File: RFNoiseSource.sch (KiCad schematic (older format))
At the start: 46 parts, among them J1 Barrel_Jack, J2 Conn_Coaxial, J3 Conn_Coaxial, Q1 2SC3356, Q2 2SC3356, Q3 2SC3356, Q4 2SC3356, Q5 2SC3356, Q6 2SC3356, U1 AMS1117-3V3

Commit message: Added LCSC part numbers, added cutout notched, added series base resistors to emitter followers
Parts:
- added C14, C15, C16: 10 nF, Capacitors_SMD:C_0805_HandSoldering, symbol C_Small
- added R19, R21, R22, R24: NC, Resistors_SMD:R_0805_HandSoldering, symbol R
- added R20, R23: 0R, Resistors_SMD:R_0805_HandSoldering, symbol R
- added R25, R26, R27: 220R, Resistors_SMD:R_0805_HandSoldering, symbol R
- R1: value 1k -> 2k2; LCSC C17513 -> C17520
- R12, R4: value 10k -> 1k; LCSC C17414 -> C17513
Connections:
- net GND: now also C14.2, C15.2, C16.1, R19.2, R21.2, R22.2, R24.2
- net at Q3.1 (B), R9.1: now also R26.1; no longer C6.1
- net at C3.2, D1.2 (A), D2.2 (A)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: now also C16.2
- net at L2.2, Q4.2 (E): now also C15.1
- net at Q5.1 (B), R13.1: now also R27.1; no longer C9.1
- net at C11.1: now also R22.1, R23.1; no longer J3.1 (In)
- net at L1.2, Q1.2 (E): now also C14.1
- net at C8.1: now also R19.1, R20.1; no longer J2.1 (In)
- net at Q6.1 (B), R16.1: now also R25.1; no longer C12.1
- new net: C6.1, R26.2
- new net: C9.1, R27.2
- new net: J3.1 (In), R23.2, R24.1
- new net: J2.1 (In), R20.2, R21.1
- new net: C12.1, R25.2
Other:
- moved on the sheet: C10, C11, C6, C9, J2, J3, Q5, R11, R12, R13, R14, R15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

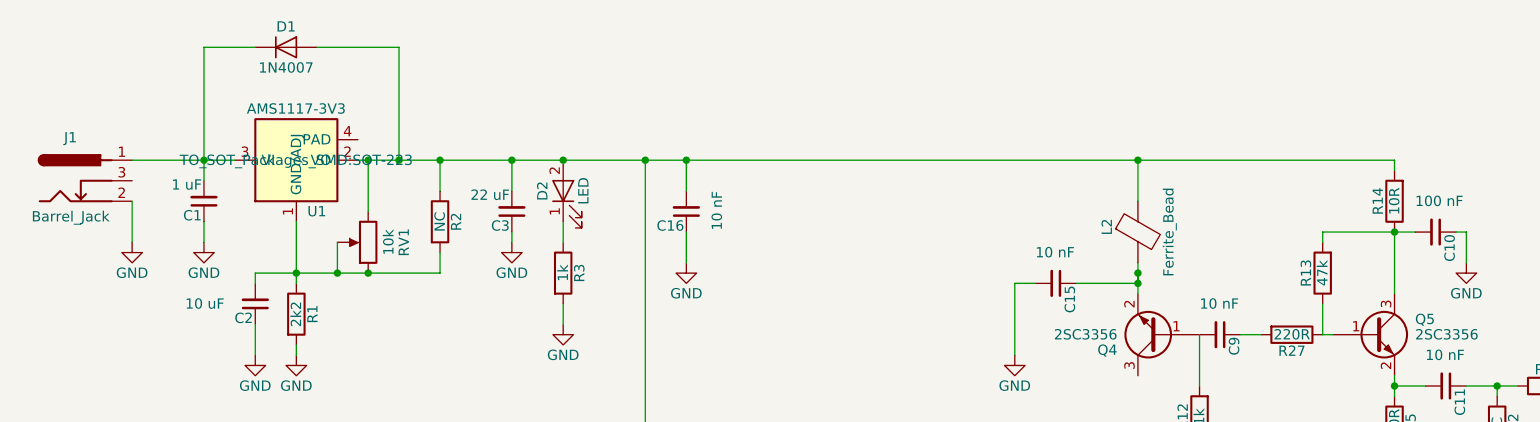
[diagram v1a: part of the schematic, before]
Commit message: Changed regulator
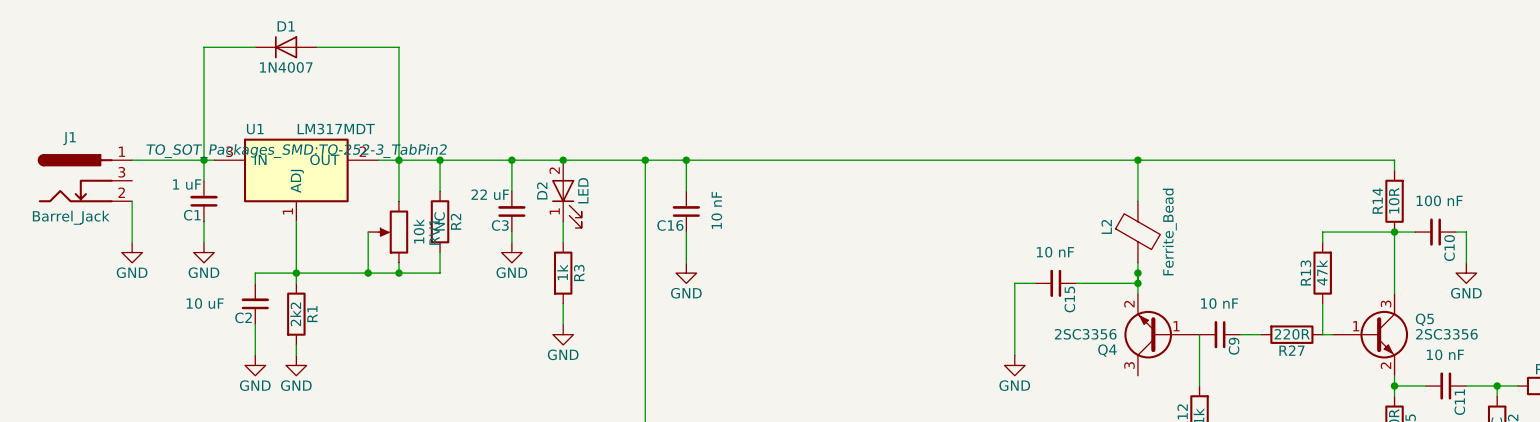
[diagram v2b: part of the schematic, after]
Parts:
- removed U1: AMS1117-3V3, TO_SOT_Packages_SMD:SOT-223, symbol AMS1117-3V3
- added U1: LM317MDT, TO_SOT_Packages_SMD:TO-252-3_TabPin2, symbol LM317MDT
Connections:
- net at C16.2, C3.2, D1.2 (A)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: now also U1.2 (OUT)
- net at C1.2, D1.1 (K), J1.1: now also U1.3 (IN)
- net at C2.2, R1.1, R2.2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: now also U1.1 (ADJ)
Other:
- moved on the sheet: RV1
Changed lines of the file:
@@
 $EndComp
 $Comp
-L GND #PWR2
+L GND #PWR01
 U 1 1 5EA1E654
 P 1700 1950
-F 0 "#PWR2" H 1700 1700 50  0001 C CNN
+F 0 "#PWR01" H 1700 1700 50  0001 C CNN
 F 1 "GND" H 1700 1800 50  0000 C CNN
 F 2 "" H 1700 1950 50  0001 C CNN
@@
 $EndComp
 $Comp
-L GND #PWR1
+L GND #PWR02
 U 1 1 5EA1E7E8
 P 1350 1950
-F 0 "#PWR1" H 1350 1700 50  0001 C CNN
+F 0 "#PWR02" H 1350 1700 50  0001 C CNN
 F 1 "GND" H 1350 1800 50  0000 C CNN
 F 2 "" H 1350 1950 50  0001 C CNN
@@
 $EndComp
 $Comp
-L GND #PWR5
+L GND #PWR03
 U 1 1 5EA1EC21
 P 2150 2500
-F 0 "#PWR5" H 2150 2250 50  0001 C CNN
+F 0 "#PWR03" H 2150 2250 50  0001 C CNN
 F 1 "GND" H 2150 2350 50  0000 C CNN
 F 2 "" H 2150 2500 50  0001 C CNN
@@
 $EndComp
 $Comp
-L GND #PWR7
+L GND #PWR04
 U 1 1 5EA1EF58
 P 3200 1950
-F 0 "#PWR7" H 3200 1700 50  0001 C CNN
+F 0 "#PWR04" H 3200 1700 50  0001 C CNN
 F 1 "GND" H 3200 1800 50  0000 C CNN
 F 2 "" H 3200 1950 50  0001 C CNN
@@
 $EndComp
 $Comp
-L GND #PWR8
+L GND #PWR05
 U 1 1 5EA1F457
 P 3450 2350
-F 0 "#PWR8" H 3450 2100 50  0001 C CNN
+F 0 "#PWR05" H 3450 2100 50  0001 C CNN
 F 1 "GND" H 3450 2200 50  0000 C CNN
 F 2 "" H 3450 2350 50  0001 C CNN
@@
 L POT RV1
 U 1 1 5EA1FA58
-P 2500 1950
-F 0 "RV1" V 2325 1950 50  0000 C CNN
-F 1 "10k" V 2400 1950 50  0000 C CNN
-F 2 "Potentiometers:Potentiometer_Triwood_RM-065" H 2500 1950 50  0001 C CNN
-F 3 "" H 2500 1950 50  0001 C CNN
-	1    2500 1950
-	-1   0    0    1
-$EndComp
-$Comp
-L AMS1117-3V3 U1
-U 1 1 5EA20303
-P 2150 1550
-F 0 "U1" H 2250 1300 50  0000 C CNN
-F 1 "AMS1117-3V3" H 2150 1800 50  0000 C CNN
-F 2 "TO_SOT_Packages_SMD:SOT-223" H 2150 1550 50  0000 C CNN
-F 3 "" H 2250 1300 50  0000 C CNN
-F 4 "LM1117 800-mA Low-Dropout Linear Regulator" H 2550 1600 61  0001 C CNN "DESC"
-F 5 "Texas Instruments" H 2350 1400 61  0001 C CNN "MFG_NAME"
-F 6 "LM1117" H 2450 1500 61  0001 C CNN "MPN"
-F 7 "C6186" H 2150 1550 60  0001 C CNN "LCSC"
-	1    2150 1550
-	1    0    0    -1
+P 2650 1900
+F 0 "RV1" V 2475 1900 50  0000 C CNN
+F 1 "10k" V 2550 1900 50  0000 C CNN
+F 2 "Potentiometers:Potentiometer_Triwood_RM-065" H 2650 1900 50  0001 C CNN
+F 3 "" H 2650 1900 50  0001 C CNN
+	1    2650 1900
+	-1   0    0    1
 $EndComp
 $Comp
@@
 $EndComp
 $Comp
-L GND #PWR3
+L GND #PWR06
 U 1 1 5EA20A42
 P 1950 2500
-F 0 "#PWR3" H 1950 2250 50  0001 C CNN
+F 0 "#PWR06" H 1950 2250 50  0001 C CNN
 F 1 "GND" H 1950 2350 50  0000 C CNN
 F 2 "" H 1950 2500 50  0001 C CNN
@@
 $EndComp
 $Comp
-L GND #PWR22
+L GND #PWR07
 U 1 1 5EA236A5
 P 7850 2050
-F 0 "#PWR22" H 7850 1800 50  0001 C CNN
+F 0 "#PWR07" H 7850 1800 50  0001 C CNN
 F 1 "GND" H 7850 1900 50  0000 C CNN
 F 2 "" H 7850 2050 50  0001 C CNN
@@
 $EndComp
 $Comp
-L GND #PWR21
+L GND #PWR08
 U 1 1 5EA23B4E
 P 7500 3150
-F 0 "#PWR21" H 7500 2900 50  0001 C CNN
+F 0 "#PWR08" H 7500 2900 50  0001 C CNN
 F 1 "GND" H 7500 3000 50  0000 C CNN
 F 2 "" H 7500 3150 50  0001 C CNN
@@
 $EndComp
 $Comp
-L GND #PWR25
+L GND #PWR09
 U 1 1 5EA24150
 P 8950 3150
-F 0 "#PWR25" H 8950 2900 50  0001 C CNN
+F 0 "#PWR09" H 8950 2900 50  0001 C CNN
 F 1 "GND" H 8950 3000 50  0000 C CNN
 F 2 "" H 8950 3150 50  0001 C CNN
@@
 $EndComp
 $Comp
-L GND #PWR19
+L GND #PWR010
 U 1 1 5EA24A07
 P 6550 3150
-F 0 "#PWR19" H 6550 2900 50  0001 C CNN
+F 0 "#PWR010" H 6550 2900 50  0001 C CNN
 F 1 "GND" H 6550 3000 50  0000 C CNN
 F 2 "" H 6550 3150 50  0001 C CNN
@@
 	1700 1000 1700 1650
 Wire Wire Line
-	1350 1550 1850 1550
-Wire Wire Line
 	1350 1950 1350 1750
 Connection ~ 1700 1550
@@
 Connection ~ 3200 1550
 Wire Wire Line
-	2500 1800 2500 1550
-Connection ~ 2500 1550
-Wire Wire Line
 	1700 1850 1700 1950
 Wire Wire Line
@@
 Connection ~ 2850 1550
 Wire Wire Line
-	2350 2100 2350 1950
-Wire Wire Line
 	1950 2100 2850 2100
 Wire Wire Line
@@
 Wire Wire Line
 	2150 1850 2150 2150
-Connection ~ 2350 2100
 Wire Wire Line
 	2150 2450 2150 2500
@@
 	1950 2500 1950 2350
 Wire Wire Line
-	2650 1550 2650 1000
+	2650 1000 2650 1750
 Wire Wire Line
 	2650 1000 2250 1000
@@
 	6250 2050 6250 2200
 Wire Wire Line
-	2450 1550 7500 1550
+	2550 1550 7500 1550
 Connection ~ 6250 1550
 Connection ~ 3450 1550
@@
 $EndComp
 $Comp
-L GND #PWR16
+L GND #PWR011
 U 1 1 5E9DA538
 P 5850 3450
-F 0 "#PWR16" H 5850 3200 50  0001 C CNN
+F 0 "#PWR011" H 5850 3200 50  0001 C CNN
 F 1 "GND" H 5850 3300 50  0000 C CNN
 F 2 "" H 5850 3450 50  0001 C CNN
@@
 $EndComp
 $Comp
-L GND #PWR14
+L GND #PWR012
 U 1 1 5E9D96E5
 P 5500 4750
-F 0 "#PWR14" H 5500 4500 50  0001 C CNN
+F 0 "#PWR012" H 5500 4500 50  0001 C CNN
 F 1 "GND" H 5500 4600 50  0000 C CNN
 F 2 "" H 5500 4750 50  0001 C CNN
@@
 $EndComp
 $Comp
-L GND #PWR13
+L GND #PWR013
 U 1 1 5E9D80F3
 P 4850 3500
-F 0 "#PWR13" H 4850 3250 50  0001 C CNN
+F 0 "#PWR013" H 4850 3250 50  0001 C CNN
 F 1 "GND" H 4850 3350 50  0000 C CNN
 F 2 "" H 4850 3500 50  0001 C CNN
@@
 $EndComp
 $Comp
-L GND #PWR12
+L GND #PWR014
 U 1 1 5E9B935A
 P 4550 4750
-F 0 "#PWR12" H 4550 4500 50  0001 C CNN
+F 0 "#PWR014" H 4550 4500 50  0001 C CNN
 F 1 "GND" H 4550 4600 50  0000 C CNN
 F 2 "" H 4550 4750 50  0001 C CNN
@@
 $EndComp
 $Comp
-L GND #PWR6
+L GND #PWR015
 U 1 1 5E9B90E6
 P 2850 4750
-F 0 "#PWR6" H 2850 4500 50  0001 C CNN
+F 0 "#PWR015" H 2850 4500 50  0001 C CNN
 F 1 "GND" H 2850 4600 50  0000 C CNN
 F 2 "" H 2850 4750 50  0001 C CNN
@@
 Connection ~ 3650 4150
 $Comp
-L GND #PWR9
+L GND #PWR016
 U 1 1 5EA2852B
 P 3650 4750
-F 0 "#PWR9" H 3650 4500 50  0001 C CNN
+F 0 "#PWR016" H 3650 4500 50  0001 C CNN
 F 1 "GND" H 3650 4600 50  0000 C CNN
 F 2 "" H 3650 4750 50  0001 C CNN
@@
 $EndComp
 $Comp
-L GND #PWR10
+L GND #PWR017
 U 1 1 5EA28D80
 P 4000 3550
-F 0 "#PWR10" H 4000 3300 50  0001 C CNN
+F 0 "#PWR017" H 4000 3300 50  0001 C CNN
 F 1 "GND" H 4000 3400 50  0000 C CNN
 F 2 "" H 4000 3550 50  0001 C CNN
@@
 $EndComp
 $Comp
-L GND #PWR4
+L GND #PWR018
 U 1 1 5EA3C1B1
 P 2000 3950
-F 0 "#PWR4" H 2000 3700 50  0001 C CNN
+F 0 "#PWR018" H 2000 3700 50  0001 C CNN
 F 1 "GND" H 2000 3800 50  0000 C CNN
 F 2 "" H 2000 3950 50  0001 C CNN
@@
 	5650 2150 5650 2500
 $Comp
-L GND #PWR15
+L GND #PWR019
 U 1 1 5EA3C75A
 P 5650 2500
-F 0 "#PWR15" H 5650 2250 50  0001 C CNN
+F 0 "#PWR019" H 5650 2250 50  0001 C CNN
 F 1 "GND" H 5650 2350 50  0000 C CNN
 F 2 "" H 5650 2500 50  0001 C CNN
@@
 $EndComp
 $Comp
-L GND #PWR11
+L GND #PWR020
 U 1 1 5EA3CCDB
 P 4050 2050
-F 0 "#PWR11" H 4050 1800 50  0001 C CNN
+F 0 "#PWR020" H 4050 1800 50  0001 C CNN
 F 1 "GND" H 4050 1900 50  0000 C CNN
 F 2 "" H 4050 2050 50  0001 C CNN
@@
 $EndComp
 $Comp
-L GND #PWR23
+L GND #PWR021
 U 1 1 5EA3D255
 P 8000 3150
-F 0 "#PWR23" H 8000 2900 50  0001 C CNN
+F 0 "#PWR021" H 8000 2900 50  0001 C CNN
 F 1 "GND" H 8000 3000 50  0000 C CNN
 F 2 "" H 8000 3150 50  0001 C CNN
@@
 $EndComp
 $Comp
-L GND #PWR24
+L GND #PWR022
 U 1 1 5EA3D4C8
 P 8450 3150
-F 0 "#PWR24" H 8450 2900 50  0001 C CNN
+F 0 "#PWR022" H 8450 2900 50  0001 C CNN
 F 1 "GND" H 8450 3000 50  0000 C CNN
 F 2 "" H 8450 3150 50  0001 C CNN
@@
 Connection ~ 8000 2650
 $Comp
-L GND #PWR20
+L GND #PWR023
 U 1 1 5EA3DE3A
 P 6950 4750
-F 0 "#PWR20" H 6950 4500 50  0001 C CNN
+F 0 "#PWR023" H 6950 4500 50  0001 C CNN
 F 1 "GND" H 6950 4600 50  0000 C CNN
 F 2 "" H 6950 4750 50  0001 C CNN
@@
 $EndComp
 $Comp
-L GND #PWR17
+L GND #PWR024
 U 1 1 5EA3DE48
 P 6000 4750
-F 0 "#PWR17" H 6000 4500 50  0001 C CNN
+F 0 "#PWR024" H 6000 4500 50  0001 C CNN
 F 1 "GND" H 6000 4600 50  0000 C CNN
 F 2 "" H 6000 4750 50  0001 C CNN
@@
 $EndComp
 $Comp
-L GND #PWR18
+L GND #PWR025
 U 1 1 5EA3DE55
 P 6450 4750
-F 0 "#PWR18" H 6450 4500 50  0001 C CNN
+F 0 "#PWR025" H 6450 4500 50  0001 C CNN
 F 1 "GND" H 6450 4600 50  0000 C CNN
 F 2 "" H 6450 4750 50  0001 C CNN
@@
 Wire Wire Line
 	6850 2400 6750 2400
+$Comp
+L LM317MDT U1
+U 1 1 5EB32B81
+P 2150 1600
+F 0 "U1" H 1950 1800 50  0000 C CNN
+F 1 "LM317MDT" H 2150 1800 50  0000 L CNN
+F 2 "TO_SOT_Packages_SMD:TO-252-3_TabPin2" H 2150 1700 50  0000 C CIN
+F 3 "" H 2150 1600 50  0000 C CNN
+F 4 "C75510" H 2150 1600 60  0001 C CNN "LCSC"
+	1    2150 1600
+	1    0    0    -1
+$EndComp
+Wire Wire Line
+	1350 1550 1750 1550
+Wire Wire Line
+	2500 1900 2500 2100
+Wire Wire Line
+	2650 2050 2650 2100
+Connection ~ 2650 2100
 $EndSCHEMATC
